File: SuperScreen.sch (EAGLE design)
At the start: 30 parts, among them CN2 JSTPH, CN3 1X4-BIG, IC2 MIC5225, Q3 BSS138, U2 MCP73831T-2ACI/OT

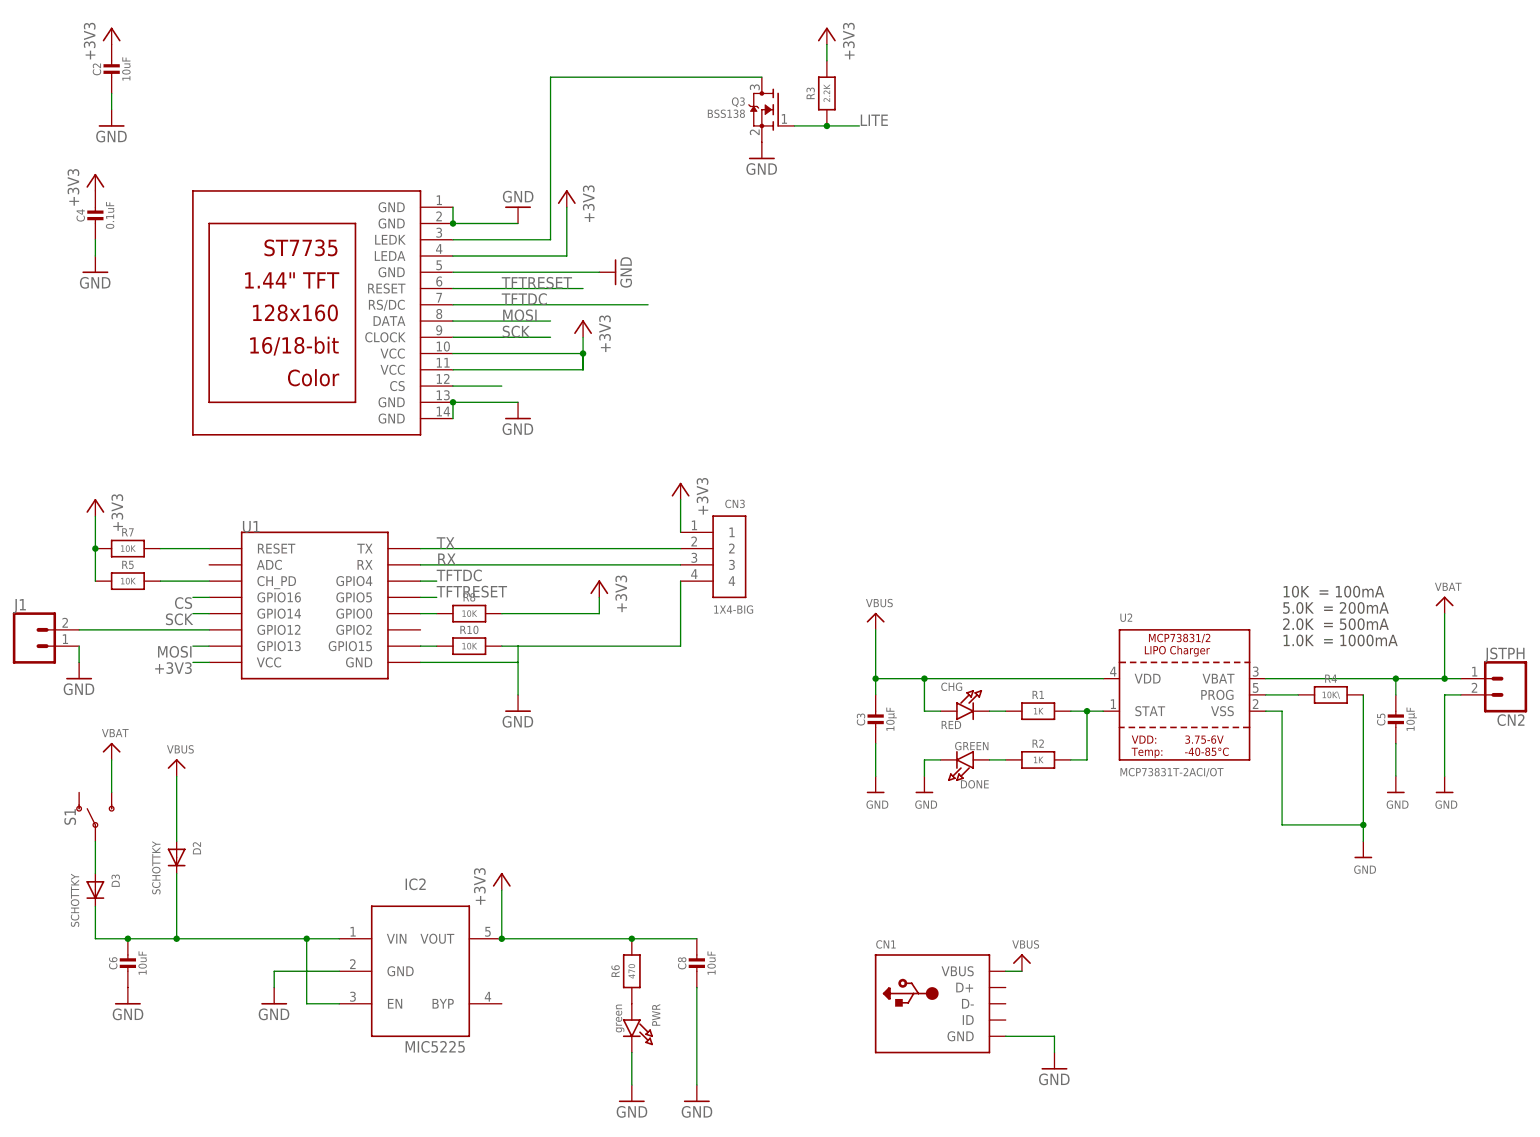
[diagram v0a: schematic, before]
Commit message: Adding in new usb connector
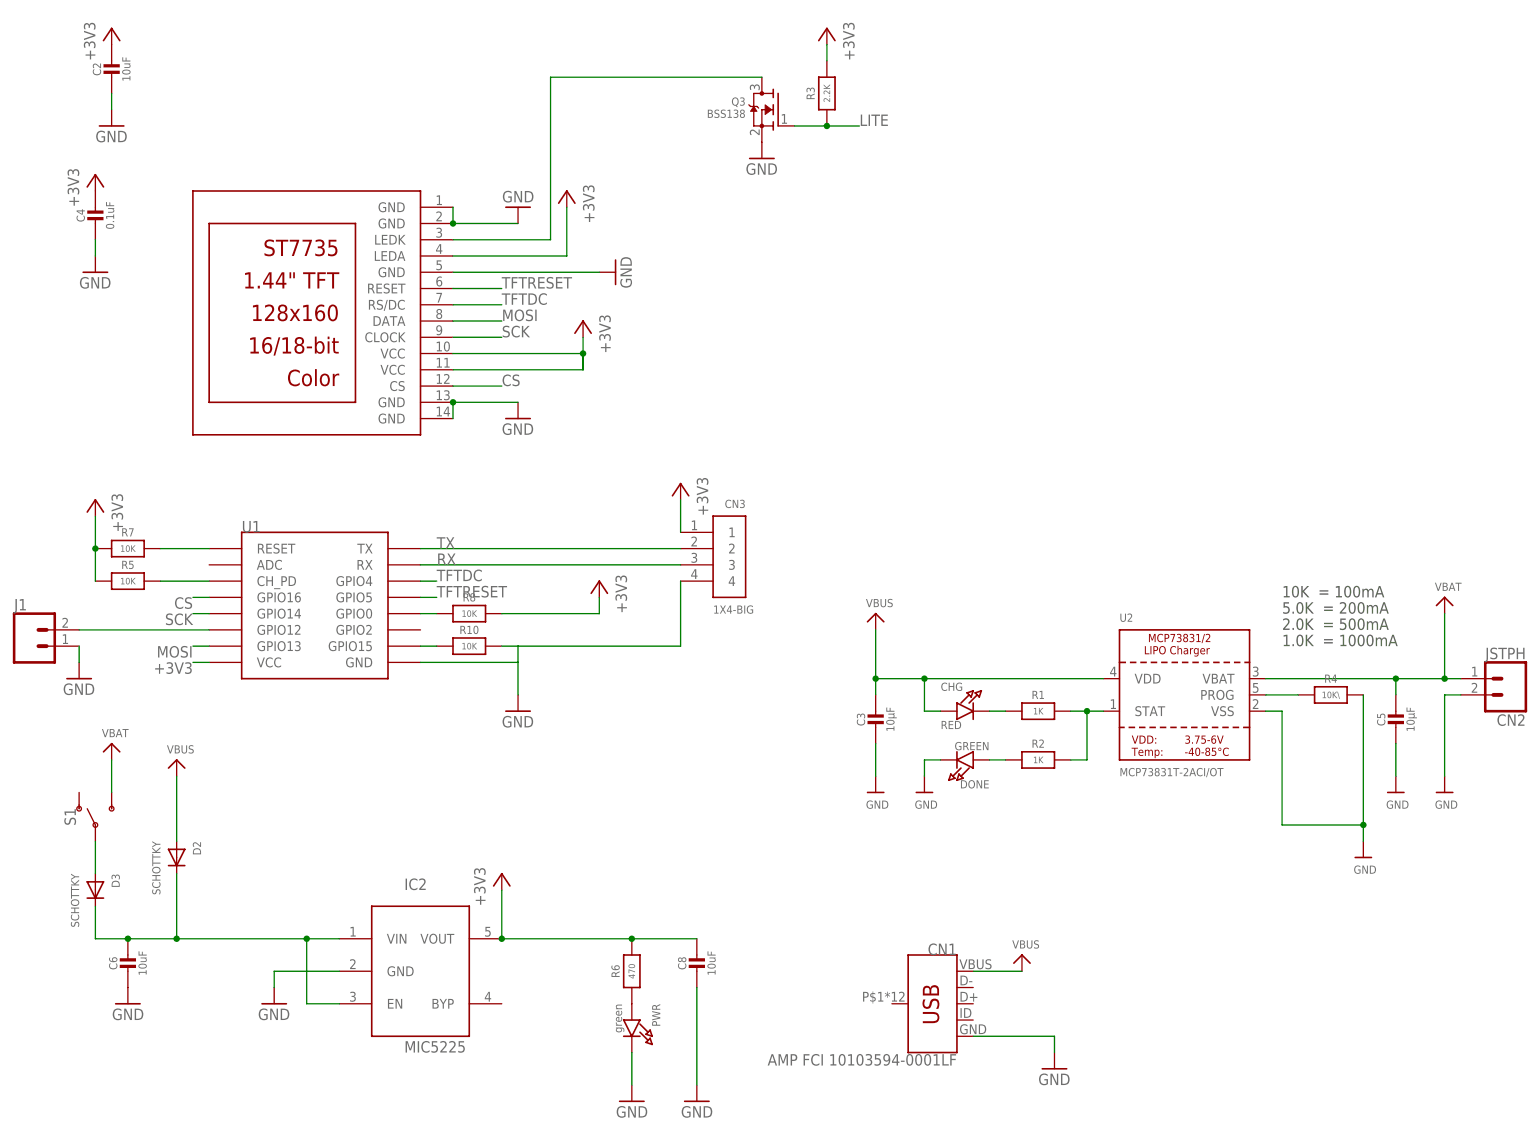
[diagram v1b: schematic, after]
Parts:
- CN1: value (none) -> AMP FCI 10103594-0001LF; device microbuilder:USBMICRO_20329 -> SparkFun-Connectors:USB_MICRO-B_HALF_PTH
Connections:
- net N$5 renamed LED-
- removed net N$7: TFT2.CS
- net CS: now also TFT2.CS
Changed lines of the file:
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@@
 <part name="GND8" library="supply1" deviceset="GND" device=""/>
 <part name="GND9" library="supply1" deviceset="GND" device=""/>
-<part name="CN1" library="microbuilder" deviceset="USB" device="MICRO_20329"/>
+<part name="CN1" library="SparkFun-Connectors" library_urn="urn:adsk.eagle:library:513" deviceset="USB_MICRO-B" device="_HALF_PTH" package3d_urn="urn:adsk.eagle:package:38241/1" value="AMP FCI 10103594-0001LF"/>
 <part name="U$10" library="microbuilder" deviceset="VBUS" device=""/>
 <part name="+3V4" library="supply1" deviceset="+3V3" device=""/>
@@
 <instance part="GND8" gate="1" x="-111.76" y="-106.68" rot="MR0"/>
 <instance part="GND9" gate="1" x="33.02" y="-116.84"/>
-<instance part="CN1" gate="G$1" x="15.24" y="-106.68"/>
+<instance part="CN1" gate="G$1" x="15.24" y="-106.68" rot="MR0"/>
 <instance part="U$10" gate="G$1" x="27.94" y="-99.06"/>
 <instance part="+3V4" gate="G$1" x="-38.1" y="-40.64" rot="MR0"/>
@@
 </segment>
 <segment>
-<wire x1="-45.72" y1="-2.54" x2="-60.96" y2="-2.54" width="0.1524" layer="91"/>
+<wire x1="-53.34" y1="-2.54" x2="-60.96" y2="-2.54" width="0.1524" layer="91"/>
 <label x="-53.34" y="-2.54" size="1.778" layer="95"/>
 <pinref part="TFT2" gate="G$1" pin="CLOCK"/>
@@
 </segment>
 <segment>
-<wire x1="-45.72" y1="0" x2="-60.96" y2="0" width="0.1524" layer="91"/>
+<wire x1="-53.34" y1="0" x2="-60.96" y2="0" width="0.1524" layer="91"/>
 <label x="-53.34" y="0" size="1.778" layer="95"/>
 <pinref part="TFT2" gate="G$1" pin="DATA"/>
@@
 </segment>
 <segment>
-<wire x1="25.4" y1="-111.76" x2="33.02" y2="-111.76" width="0.1524" layer="91"/>
+<wire x1="20.32" y1="-111.76" x2="33.02" y2="-111.76" width="0.1524" layer="91"/>
 <wire x1="33.02" y1="-111.76" x2="33.02" y2="-114.3" width="0.1524" layer="91"/>
 <pinref part="GND9" gate="1" pin="GND"/>
@@
 </segment>
 </net>
-<net name="N$5" class="0">
+<net name="LED-" class="1">
 <segment>
 <wire x1="-45.72" y1="38.1" x2="-12.7" y2="38.1" width="0.1524" layer="91"/>
@@
 </segment>
 <segment>
-<wire x1="-30.48" y1="2.54" x2="-60.96" y2="2.54" width="0.1524" layer="91"/>
+<wire x1="-53.34" y1="2.54" x2="-60.96" y2="2.54" width="0.1524" layer="91"/>
 <label x="-53.34" y="2.54" size="1.778" layer="95"/>
 <pinref part="TFT2" gate="G$1" pin="RS/DC"/>
@@
 <net name="TFTRESET" class="0">
 <segment>
-<wire x1="-40.64" y1="5.08" x2="-60.96" y2="5.08" width="0.1524" layer="91"/>
+<wire x1="-53.34" y1="5.08" x2="-60.96" y2="5.08" width="0.1524" layer="91"/>
 <label x="-53.34" y="5.08" size="1.778" layer="95"/>
 <pinref part="TFT2" gate="G$1" pin="RESET"/>
@@
 <wire x1="-99.06" y1="-43.18" x2="-101.6" y2="-43.18" width="0.1524" layer="91"/>
 <label x="-101.6" y="-43.18" size="1.778" layer="95" rot="R180"/>
+</segment>
+<segment>
+<pinref part="TFT2" gate="G$1" pin="CS"/>
+<wire x1="-60.96" y1="-10.16" x2="-53.34" y2="-10.16" width="0.1524" layer="91"/>
+<label x="-53.34" y="-10.16" size="1.778" layer="95"/>
 </segment>
 </net>
@@
 <wire x1="-66.04" y1="-35.56" x2="-25.4" y2="-35.56" width="0.1524" layer="91"/>
 <pinref part="CN3" gate="G$1" pin="2"/>
-</segment>
-</net>
-<net name="N$7" class="0">
-<segment>
-<pinref part="TFT2" gate="G$1" pin="CS"/>
-<wire x1="-60.96" y1="-10.16" x2="-53.34" y2="-10.16" width="0.1524" layer="91"/>
 </segment>
 </net>
@@
 <pinref part="CN1" gate="G$1" pin="VBUS"/>
 <pinref part="U$10" gate="G$1" pin="VBUS"/>
-<wire x1="27.94" y1="-101.6" x2="25.4" y2="-101.6" width="0.1524" layer="91"/>
-</segment>
-</net>
+<wire x1="27.94" y1="-101.6" x2="20.32" y2="-101.6" width="0.1524" layer="91"/>
+</segment>
+</net>

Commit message: R1 Ordered from OshPark
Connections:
- net GND: now also CN1.SHIELD
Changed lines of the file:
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@@
 <part name="S1" library="SparkFun-Switches" library_urn="urn:adsk.eagle:library:535" deviceset="SWITCH-SPDT" device="-SMD-RIGHT-ANGLE" package3d_urn="urn:adsk.eagle:package:40179/1"/>
 <part name="R6" library="microbuilder" deviceset="RESISTOR" device="0805_NOOUTLINE" value="470"/>
+<part name="GND14" library="supply1" deviceset="GND" device=""/>
 </parts>
 <sheets>
@@
 <instance part="S1" gate="1" x="-116.84" y="-78.74" rot="R90"/>
 <instance part="R6" gate="G$1" x="-33.02" y="-101.6" rot="R90"/>
+<instance part="GND14" gate="1" x="0" y="-109.22"/>
 </instances>
 <busses>
@@
 <wire x1="-119.38" y1="-50.8" x2="-119.38" y2="-53.34" width="0.1524" layer="91"/>
 </segment>
-</net>
+<segment>
+<pinref part="GND14" gate="1" pin="GND"/>
+<pinref part="CN1" gate="G$1" pin="SHIELD"/>
+<wire x1="0" y1="-106.68" x2="7.62" y2="-106.68" width="0.1524" layer="91"/>
+</segment>
+</net>
